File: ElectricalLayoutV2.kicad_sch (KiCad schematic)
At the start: 52 parts, among them K1 Coil: 24V, Contact: 40A, K2 Relay_SPST-NO, K3 Relay_SPST-NO, K4 Relay_SPST-NO, SW1 SW_Push, SW3 SW_Push, SW4 SW_Push, SW5 SW_Push, U1 DS18B20, U2 DS18B20, U3 DS18B20, U4 DS18B20, U5 DS18B20

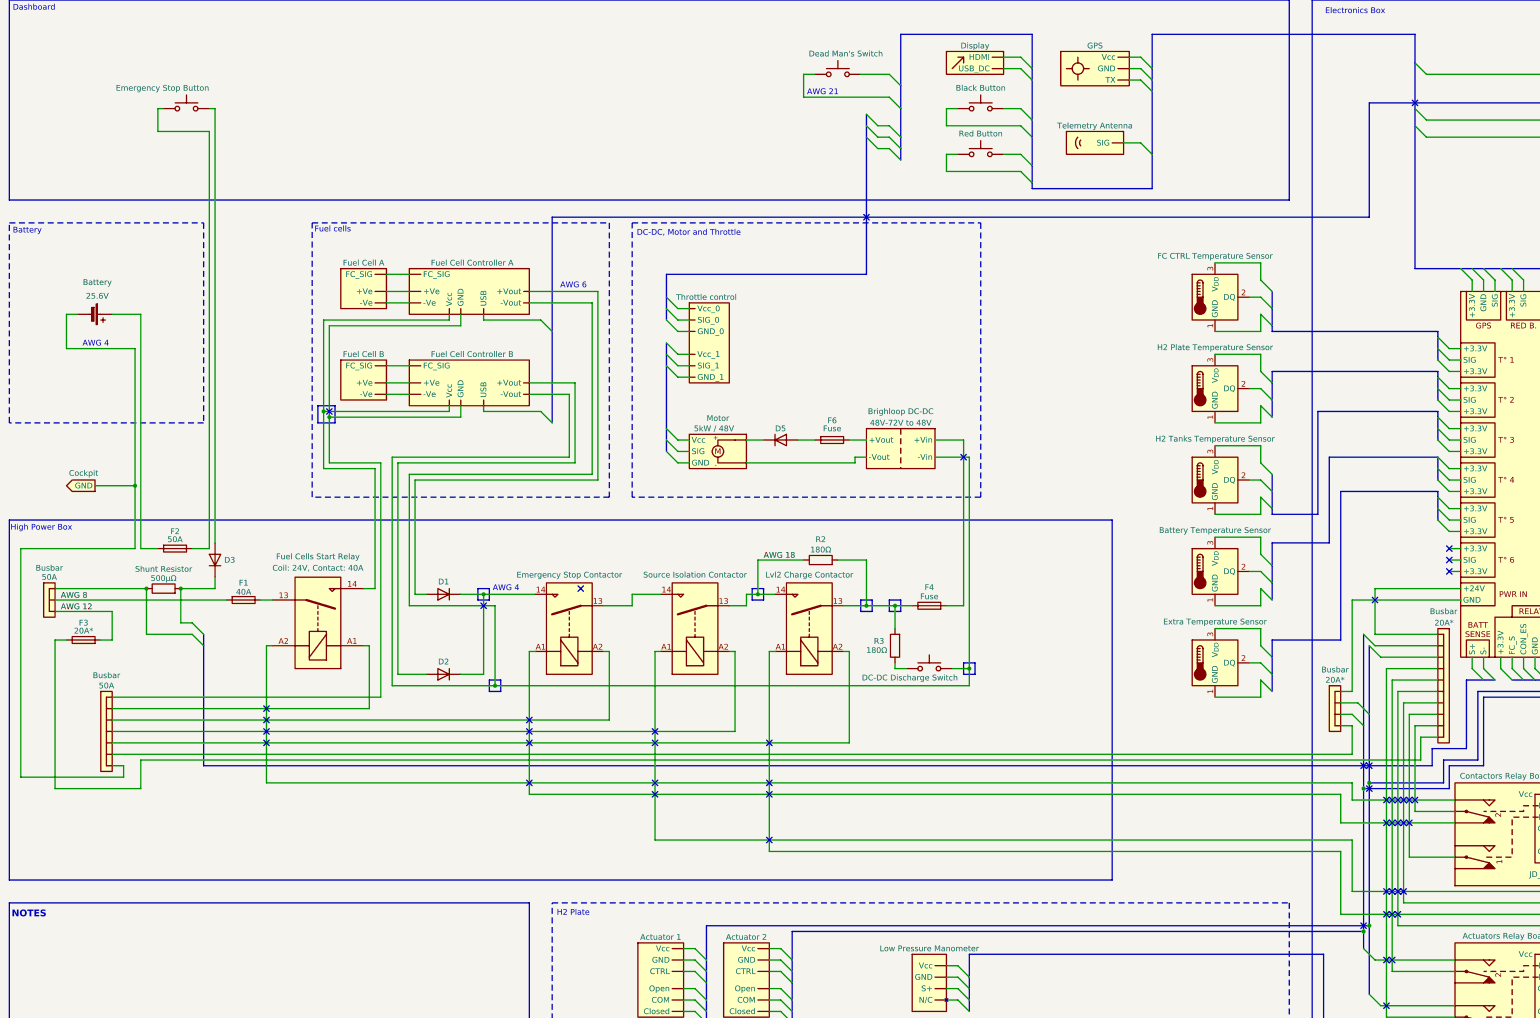
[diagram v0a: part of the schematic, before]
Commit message: Move high power box to separate sheet
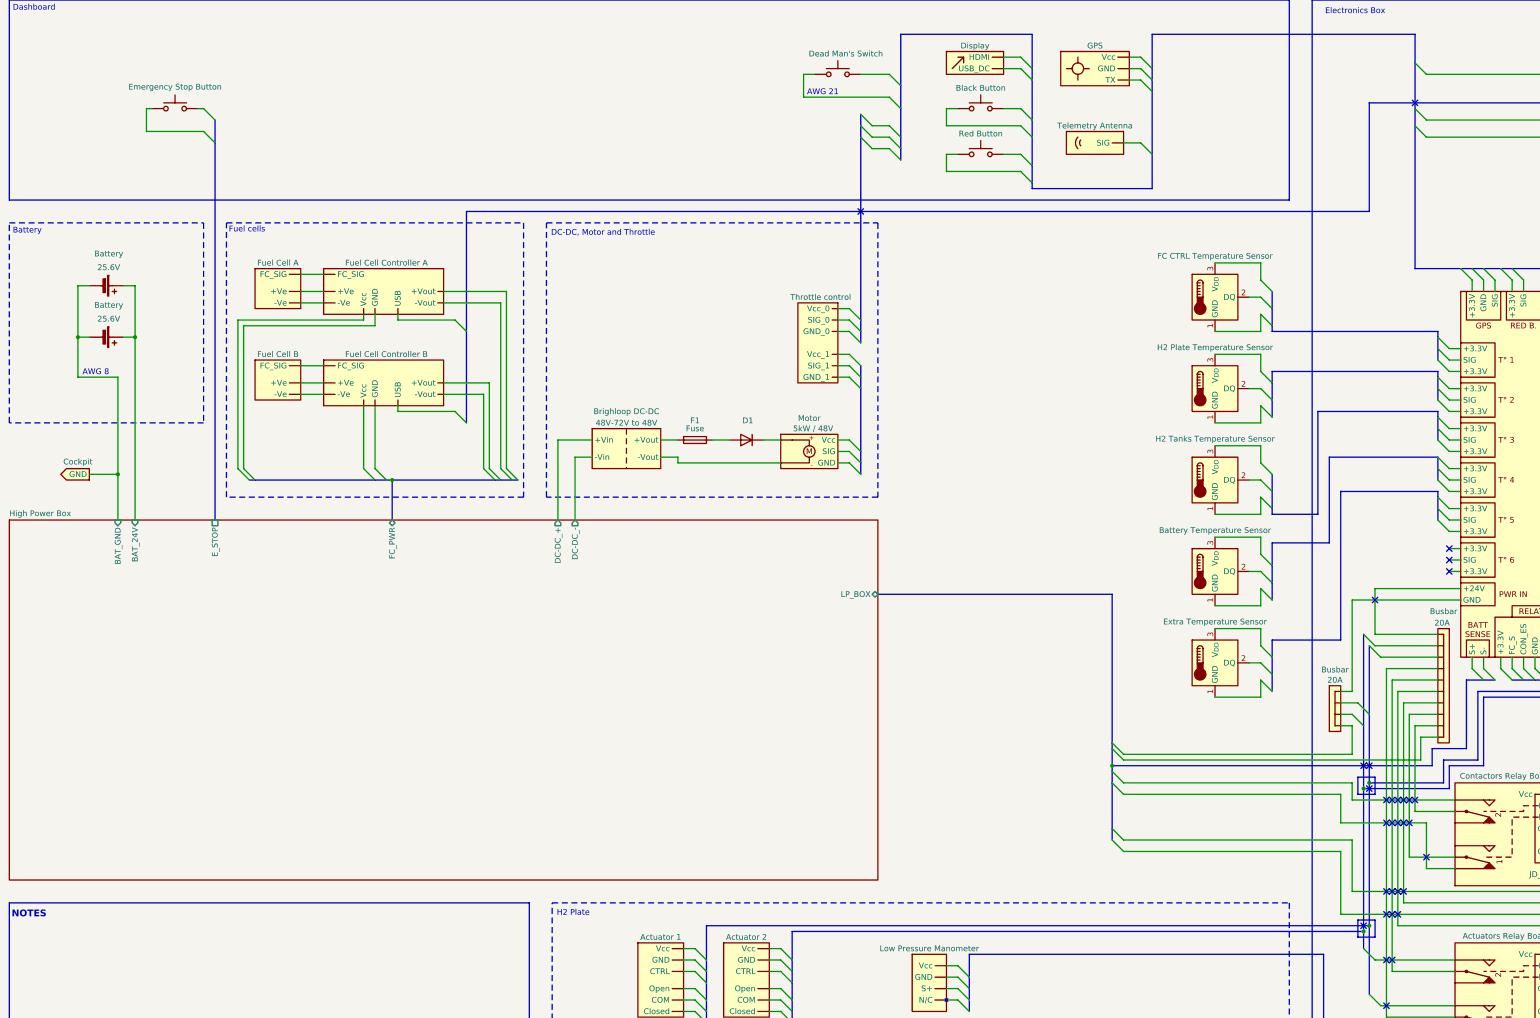
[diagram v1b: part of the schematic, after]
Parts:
- removed BSB1: 50A, symbol Exocet_Electrical:Busbar_3
- removed BSB2: 50A, symbol Exocet_Electrical:Busbar_7
- removed D2, D3, D5: D, symbol Device:D
- removed F2: 50A, symbol Device:Fuse
- removed F3: 20A*, symbol Device:Fuse
- removed F4, F6: Fuse, symbol Device:Fuse
- removed K1: Coil: 24V, Contact: 40A, Relay_THT:Relay_SPST_RAYEX-L90AS, symbol Relay:RAYEX-L90AS
- removed K2, K3, K4: Relay_SPST-NO, symbol Relay:Relay_SPST-NO
- removed R1: 500µΩ, symbol Device:R
- removed R2, R3: 180Ω, symbol Device:R
- removed SW3: SW_Push, symbol Switch:SW_Push
- added B1: 25.6V, symbol Device:Battery_Cell
- BSB3, BSB4: value 20A* -> 20A
- F1: value 40A -> Fuse
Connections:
- net High Power Box/BAT_24V: now reaches B2.1 (+)
- net High Power Box/BAT_24V: now also B1.1 (+)
- net at RELB3. (Vcc): now also BSB4.
- net at BSB4.: no longer RELB3. (Vcc)
- net at FCC2. (Vcc): no longer FC3. (FC_SIG)
- net at F1.1: now also D1.2 (A)
- net at BSB3.: now also PCB1. (SIG)
- net at PCB1. (SIG): now also BSB4.; no longer BSB3.
- net at PROP1. (Vcc): now also D1.1 (K)
- net at RELB1. (Vcc): now also BSB4.
- net High Power Box/DC-DC_-: now reaches DCC1. (-Vout)
- net at RELB2. (Vcc): now also BSB4.
- net at FCC1. (Vcc): now also FC4. (FC_SIG)
- net High Power Box/BAT_GND: now reaches B2.2 (-), CGND1. (GND)
- net High Power Box/BAT_GND: now also B1.2 (-)
- net at RPI1. (USBv3_1): now also ARD1. (USB)
- net at ARD1. (USB): no longer RPI1. (USBv3_1)
- net AWG 8: no longer names the net of F1.2
- net AWG 8: now also DCC1. (-Vout)
- new net: BSB4., RELB3. (Vcc)
- new net: FC3. (FC_SIG), FCC2. (Vcc) (x2)
- new net: BSB4., RELB1. (Vcc)
- new net: DCC1. (-Vout), PROP1. (Vcc)
- new net: FC4. (FC_SIG), FCC1. (Vcc) (x2)
- new net: PCB1. (SIG), RPI1. (USBv3_1)
- new net: BSB4., RELB2. (Vcc)
- new net High Power Box/DC-DC_+: DCC1. (-Vout)
- now unconnected: BSB4., BSB4., BSB4., BSB4., BSB4., BSB4., BSB4., FCC2. (Vcc), FCC2. (Vcc), FCC2. (Vcc), FCC2. (Vcc), FCC2. (Vcc)
- no-connect marks 53 -> 34
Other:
- added sheet High Power Box (high_power_box.kicad_sch)
- note added: "AWG 8"
- note removed: "AWG 4"
- note removed: "AWG 6"
- note removed: "High Power Box"

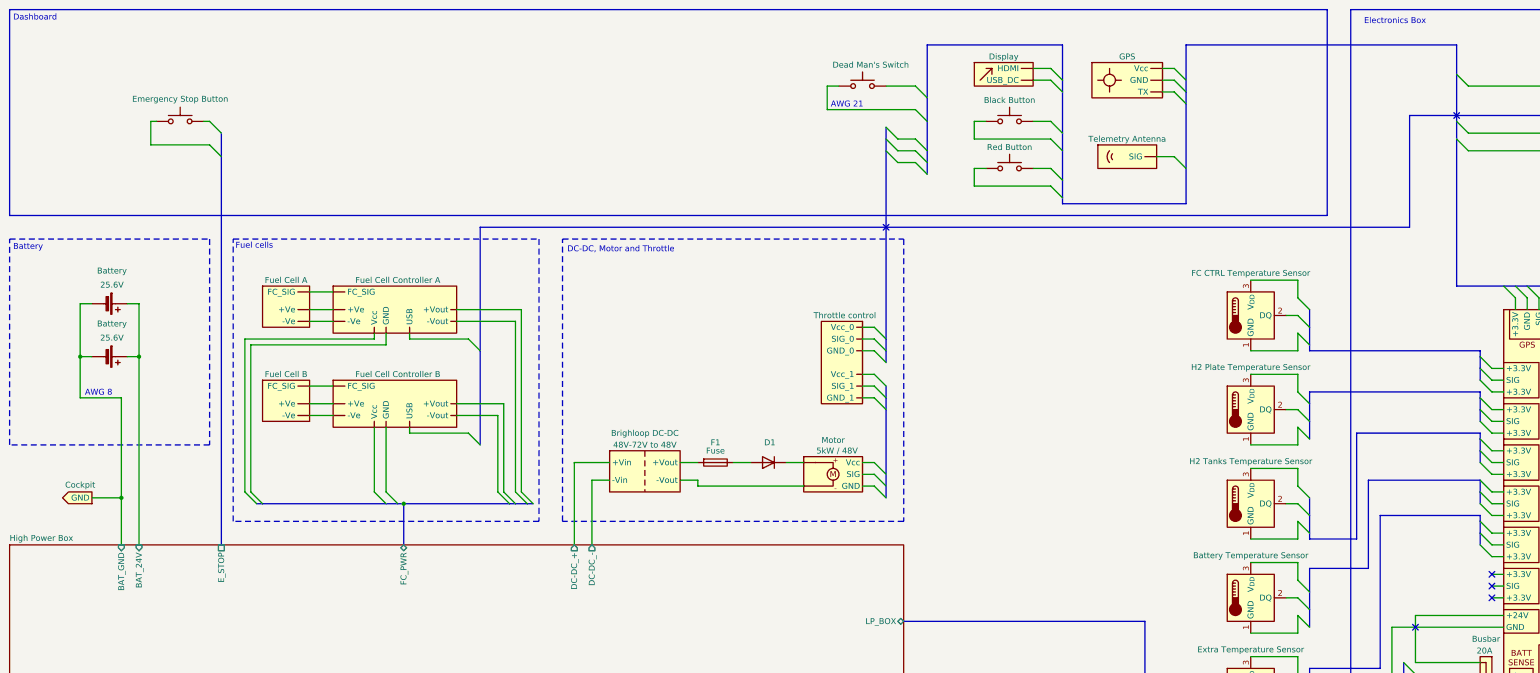
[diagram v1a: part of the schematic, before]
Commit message: Move Dashboard to its own page
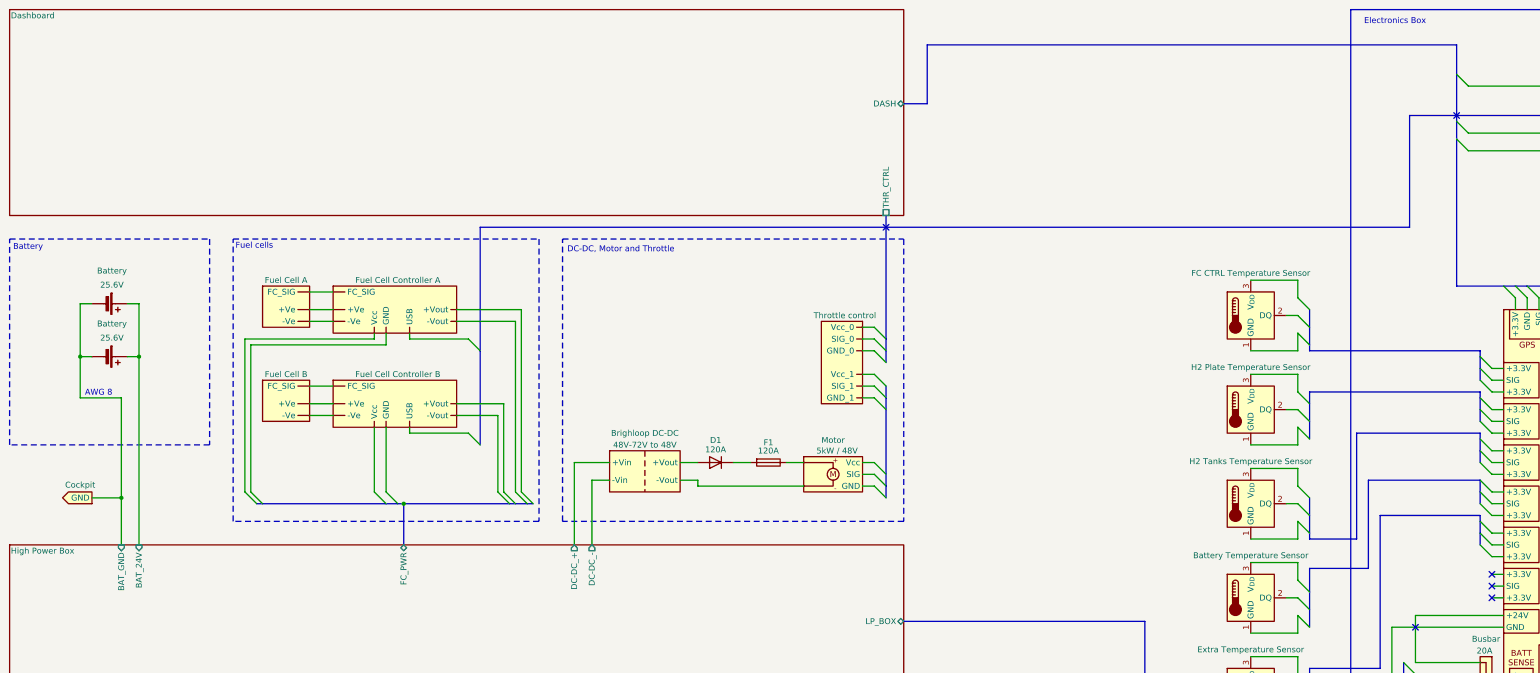
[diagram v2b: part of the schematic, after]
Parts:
- removed ANT1: ~, symbol Exocet_Electrical:Antenna
- removed DSP1: ~, symbol Exocet_Electrical:Display
- removed GPS1: ~, symbol Exocet_Electrical:GPS
- removed SW1, SW4, SW5: SW_Push, symbol Switch:SW_Push
- removed SW2: ~, symbol Switch:SW_Push
- D1: value D -> 120A
- F1: value Fuse -> 120A
- renumbered BSB3 to BSB1, BSB4 to BSB2, FC3 to FC1, FC4 to FC2, FCC2 to FCC1, FCC1 to FCC2, MAN2 to MAN1, MAN1 to MAN2, RELB3 to RELB1, RELB1 to RELB2, RELB2 to RELB3
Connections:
- net at RELB1. (Vcc): now also BSB2.
- net at BSB2.: no longer RELB1. (Vcc)
- net at FCC1. (Vcc): no longer FC1. (FC_SIG)
- net at BSB1.: now also PCB1. (SIG)
- net at PCB1. (SIG): now also BSB2.; no longer BSB1.
- net at RELB2. (Vcc): now also BSB2.
- net at F1.1: now also PROP1. (Vcc); no longer D1.2 (A)
- net at F1.2: now also D1.1 (K); no longer DCC1. (-Vout)
- net at PROP1. (Vcc): now also DCC1. (-Vout)
- net at FCC2. (Vcc): now also FC2. (FC_SIG)
- net at RPI1. (USBv3_1): now also ARD1. (USB)
- net at ARD1. (USB): no longer RPI1. (USBv3_1)
- net at RELB3. (Vcc): now also BSB2.
- new net: BSB2., RELB1. (Vcc)
- new net: FC1. (FC_SIG), FCC1. (Vcc) (x2)
- new net: D1.2 (A), DCC1. (-Vout)
- new net: BSB2., RELB2. (Vcc)
- new net: FC2. (FC_SIG), FCC2. (Vcc) (x2)
- new net: PCB1. (SIG), RPI1. (USBv3_1)
- new net: BSB2., RELB3. (Vcc)
- now unconnected: BSB2., BSB2., BSB2., BSB2., BSB2., BSB2., FCC1. (Vcc)
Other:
- added sheet Dashboard (dashboard.kicad_sch)
- sheet High Power Box ports: added none; removed E_STOP
- note removed: "AWG 21"
- note removed: "Dashboard"

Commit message: Start low power box sheet
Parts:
- removed ARD1: ~, symbol Exocet_Electrical:Arduino
- removed BSB1: 20A, symbol Exocet_Electrical:Busbar_4
- removed BSB2: 20A, symbol Exocet_Electrical:Busbar_10
- removed D1: 120A, symbol Device:D
- removed PCB1: ~, symbol Exocet_Electrical:PCB
- removed RELB1, RELB2, RELB3: ~, symbol Exocet_Electrical:Relay_Board
- removed RPI1: ~, symbol Exocet_Electrical:Raspberry_Pi
- added BRC1: ~, symbol Exocet_Electrical:Brake_Chopper
- B1: Name Battery -> Battery 1
- B2: Name Battery -> Battery 2
- DCC1: Name Brighloop DC-DC -> BrightLoop DC-DC
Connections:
- net at F1.2: now also BRC1.
- net at FCC1. (Vcc): no longer FC1. (FC_SIG)
- net at PROP1. (Vcc): now also DCC1. (-Vout)
- net at FCC2. (Vcc): now also FC2. (FC_SIG)
- new net: FC1. (FC_SIG), FCC1. (Vcc) (x2)
- new net: BRC1., DCC1. (-Vout)
- new net: FC2. (FC_SIG), FCC2. (Vcc) (x2)
- now unconnected: FCC1. (Vcc)
- no-connect marks 34 -> 0
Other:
- added sheet Low Power Box (low_power_box.kicad_sch)
- sheet Dashboard ports: added none; removed THR_CTRL
- note removed: "Electronics Box"
- moved on the sheet: F1

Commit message: Complete Low Power Box
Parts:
- removed U5: DS18B20, Package_TO_SOT_THT:TO-92_Inline, symbol Sensor_Temperature:DS18B20
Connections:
- net at FCC1. (Vcc): no longer FC1. (FC_SIG)
- net at PROP1. (Vcc): now also DCC1. (-Vout)
- net at FCC2. (Vcc): now also FC2. (FC_SIG)
- new net: FC1. (FC_SIG), FCC1. (Vcc) (x2)
- new net: FC2. (FC_SIG), FCC2. (Vcc) (x2)
- now unconnected: FCC1. (Vcc)
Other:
- sheet Low Power Box ports: added none; removed TEMP_4, TEMP_5

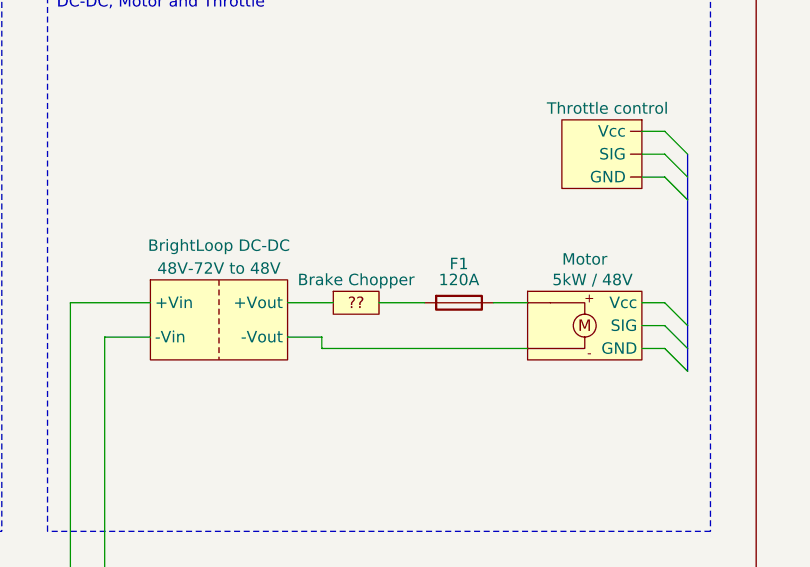
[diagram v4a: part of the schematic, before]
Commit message: Remove Brake Chopper
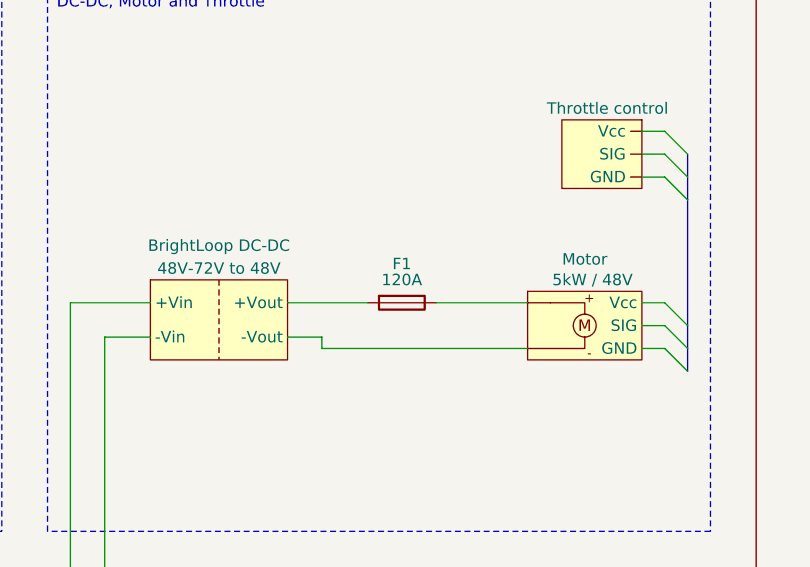
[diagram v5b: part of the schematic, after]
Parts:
- removed BRC1: ~, symbol Exocet_Electrical:Brake_Chopper
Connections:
- net at F1.2: now also DCC1. (-Vout)
- net at FCC1. (Vcc): no longer FC1. (FC_SIG)
- net at PROP1. (Vcc): now also DCC1. (-Vout)
- net at FCC2. (Vcc): now also FC2. (FC_SIG)
- new net: FC1. (FC_SIG), FCC1. (Vcc) (x2)
- new net: FC2. (FC_SIG), FCC2. (Vcc) (x2)
- now unconnected: FCC1. (Vcc)
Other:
- moved on the sheet: F1

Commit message: Finalize layout
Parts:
- added D1: D, symbol Device:D
- added R4: 4.8kΩ, symbol Device:R
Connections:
- net at F1.2: now also D1.1 (K), R4.1; no longer DCC1. (-Vout)
- net at FCC1. (Vcc): no longer FC1. (FC_SIG)
- net at PROP1. (Vcc): now also DCC1. (-Vout), R4.2
- net at FCC2. (Vcc): now also FC2. (FC_SIG)
- new net: FC1. (FC_SIG), FCC1. (Vcc) (x2)
- new net: FC2. (FC_SIG), FCC2. (Vcc) (x2)
- new net: D1.2 (A), DCC1. (-Vout)
- now unconnected: FCC1. (Vcc)
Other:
- moved on the sheet: F1
